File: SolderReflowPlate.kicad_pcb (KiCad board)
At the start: 2 copper layers, 44 parts, among them J1 Barrel_Jack_Switch, J2 Conn_01x02, J3 USB_B_Micro, Q1 WSP4409A, Q2 IRLR8726TRPBF, U1 INA219AIDR, U2 AMS1117-3.3, U3 W25Q128JVS, U4 RP2040, Y1 HCM4912000000ABJT

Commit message: WIP: added LCSC part numbers
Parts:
- removed U2: AMS1117-3.3, Package_TO_SOT_SMD:SOT-223-3_TabPin2
- added D2: SS54, Diode_SMD:D_SMA, F.Cu at (152.9, 78.2)
- added D3: SS54, Diode_SMD:D_SMA, F.Cu at (155.1, 84.0)
- added U5: HT7533-1, Package_TO_SOT_SMD:SOT-89-3, F.Cu at (157.5, 73.0)
- C1, C2: value 680uF 16V -> 680uF 35V
- D1: value SS36-E3/57T -> SS54
- Q1: value WSP4409A -> FDS4141-NL-VB
- moved C18 8.06 mm to (158.9, 79.2), turned to -90 degrees
- moved C5 4.66 mm to (156.2, 79.2), turned to -90 degrees
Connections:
- net Net-(Q2-G) renamed /POWER/FET_PWM
- C5 pad 1: VBUS -> Net-(D2-K)
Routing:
- net Net-(D2-K): track 0.00 -> 12.0 mm
- net GND: track 30.2 -> 34.8 mm, vias 20 -> 22
- net +3V3: track 43.8 -> 47.1 mm, vias 2 -> 4
- net VBUS: track 2.11 -> 5.19 mm
- removed copper zone on F.Cu, net VBUS

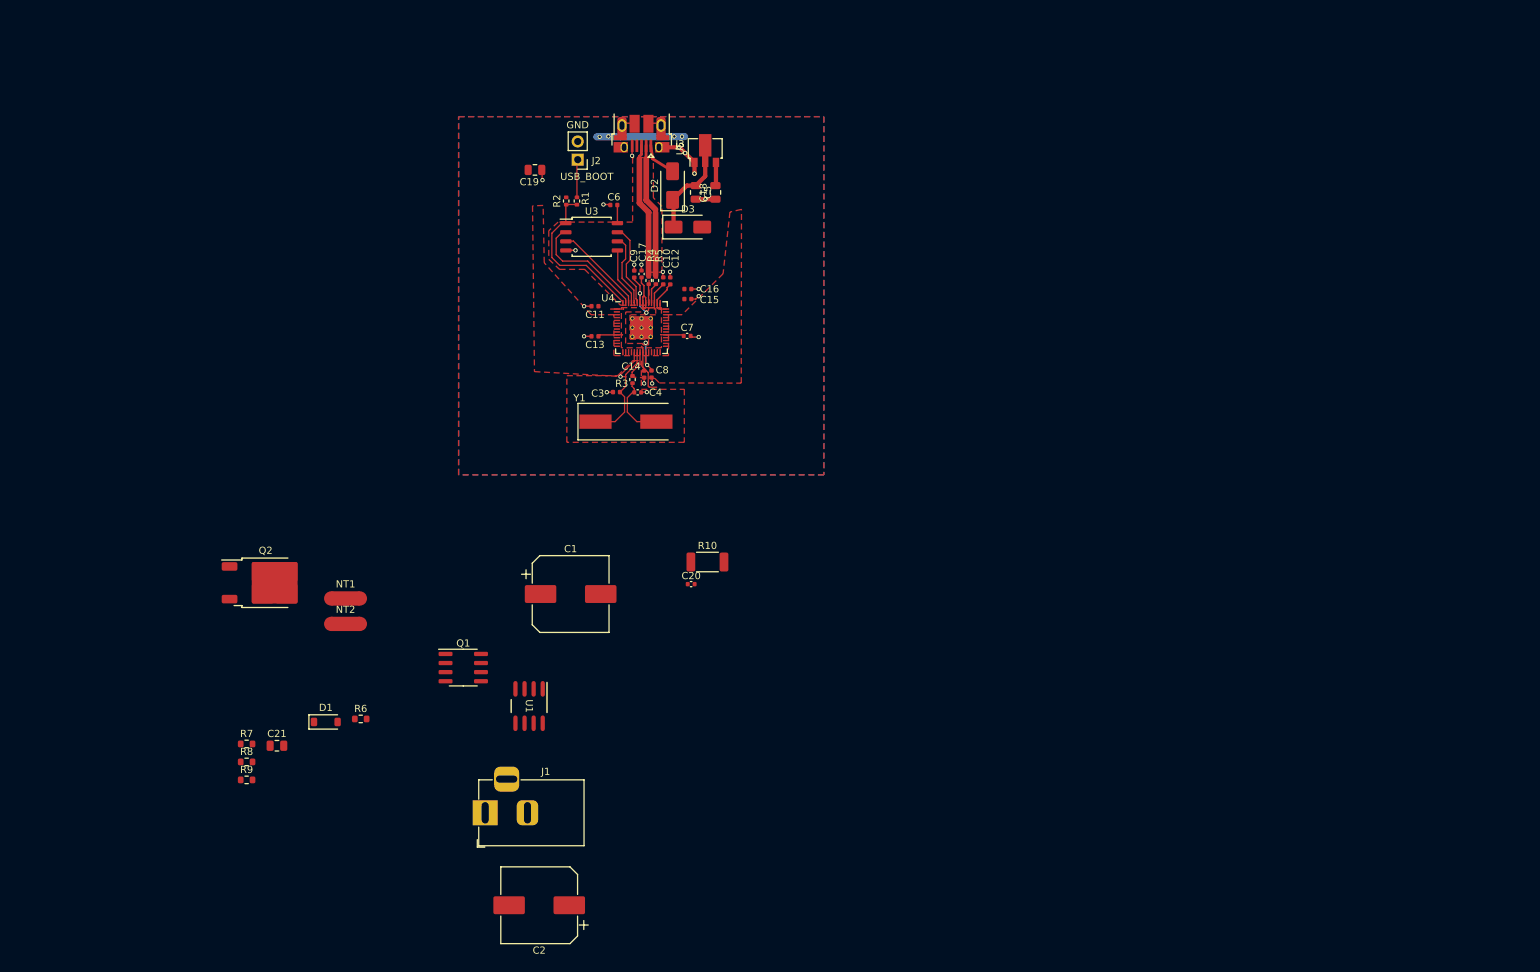
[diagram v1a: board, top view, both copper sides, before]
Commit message: WIP: cleaned up top 3V3 pour
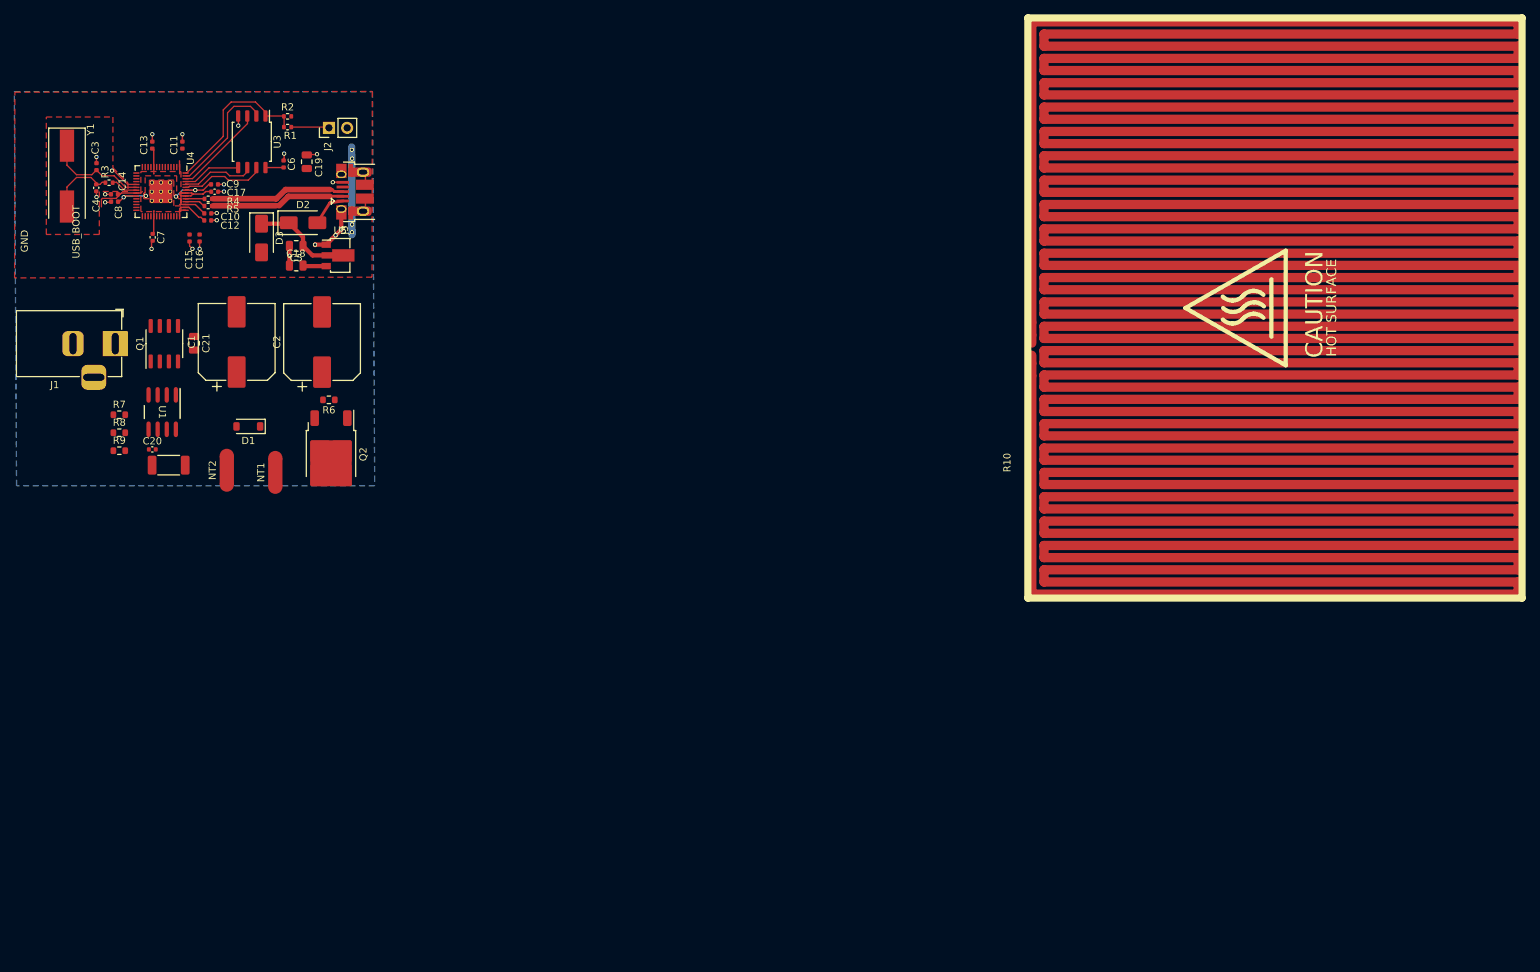
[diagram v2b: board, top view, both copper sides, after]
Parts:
- added NT1: NetTie_2, NetTie:NetTie-2_SMD_Pad1.3mm, F.Cu at (203.1, 103.9)
- added NT2: NetTie_2, NetTie:NetTie-2_SMD_Pad1.3mm, F.Cu at (203.1, 98.2)
- moved Y1 85.2 mm to (68.4, 76.9), turned to -90 degrees
- moved C2 84.3 mm to (104.0, 100.1), turned to 90 degrees
- moved J1 83.4 mm to (75.1, 100.3), turned to 0 degrees
- moved C4 80.8 mm to (72.5, 78.6), turned to -90 degrees
- moved C3 79.1 mm to (72.5, 75.6), turned to 90 degrees
- moved C8 78.7 mm to (75.0, 80.5), turned to 180 degrees
- moved C14 78.1 mm to (75.0, 79.5), turned to 180 degrees
- moved R3 78.1 mm to (74.3, 77.8), turned to 180 degrees
- moved C20 77.5 mm to (80.3, 115.1)
- moved R10 76.4 mm to (82.6, 117.3), turned to 180 degrees
- moved C7 75.9 mm to (80.4, 85.5), turned to -90 degrees
- moved C15 70.1 mm to (85.5, 85.6), turned to -90 degrees
- moved U4 69.7 mm to (81.5, 79.1), turned to -90 degrees
- moved C16 68.5 mm to (86.9, 85.6), turned to -90 degrees
- moved C13 67.3 mm to (80.3, 72.6), turned to 90 degrees
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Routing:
- net HEATPLATE: track 0.00 -> 3333.3 mm
- net (no net): track 0.00 -> 2.20 mm
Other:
- board text added: "CAUTION"
- board text added: "HOT SURFACE"
